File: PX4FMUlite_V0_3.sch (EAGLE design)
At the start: 155 parts, among them J2 DF13-4P-1.25V, J201 DF13C-6P-1.25V, J202 DF13C-6P-1.25V, J203 DF13C-6P-1.25V, J3 DF13C-4P-1.25V, J302 DF13C-4P-1.25V, J401 DF13C-4P-1.25V, J403 DF13C-7P-1.25V, J405 DF13C-4P-1.25V, J801 JST-ZH-3, J802 DF13C-3P-1.25V, M3_MOUNT1101 MOUNT-HOLE3.1MM, M3_MOUNT1102 MOUNT-HOLE3.1MM, M3_MOUNT1103 MOUNT-HOLE3.1MM, M3_MOUNT1104 MOUNT-HOLE3.1MM, U101 STM32F4X7VX, U2 MAX3051, U401 MAX3051, U903 74LVC2G240, X101 3.2x2.5 mm / 24 MHz / 15 ppm

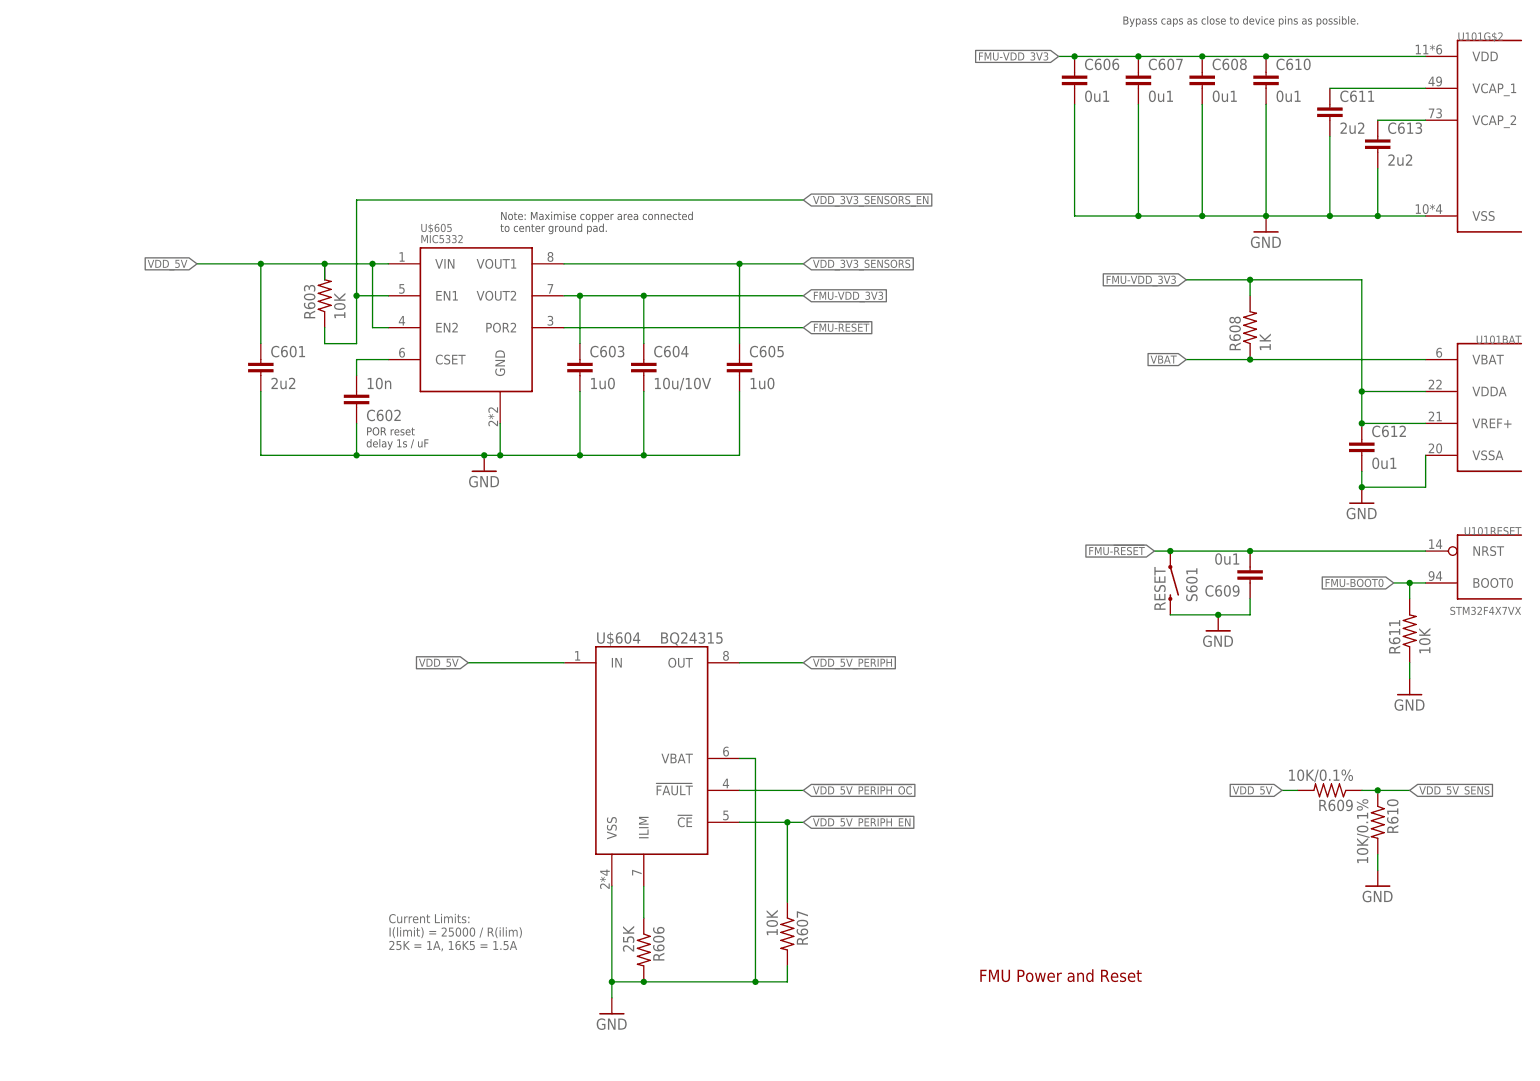
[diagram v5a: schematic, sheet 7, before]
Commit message: LDO shuffle. VBUS reconnected
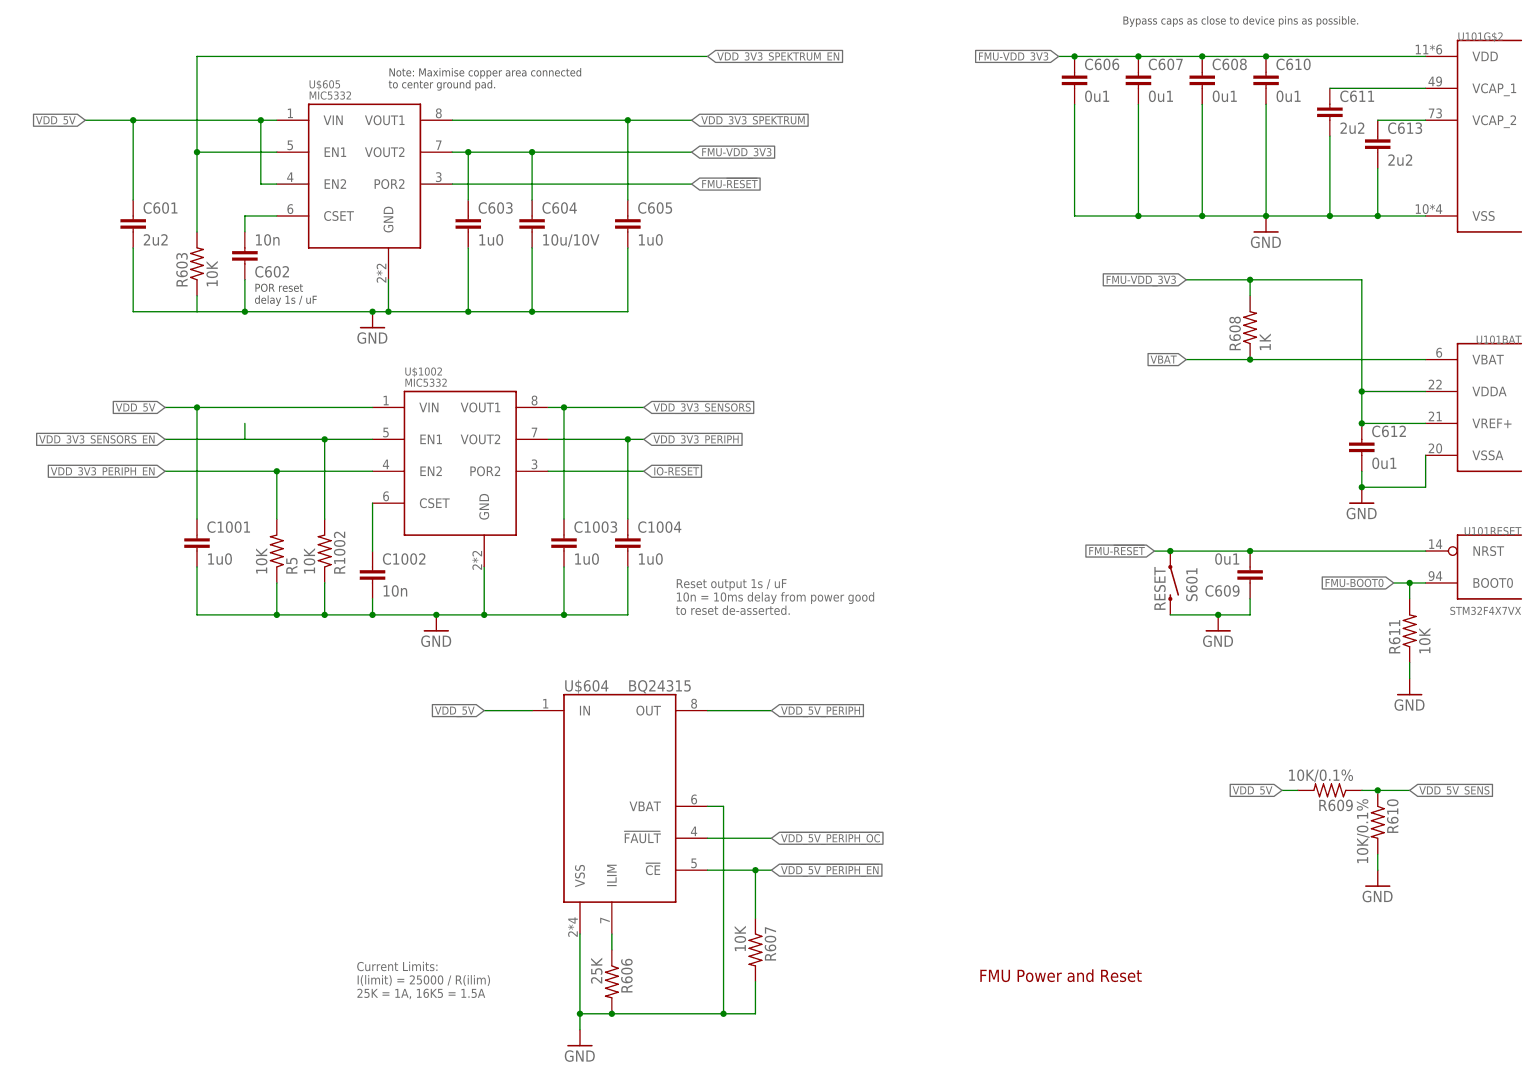
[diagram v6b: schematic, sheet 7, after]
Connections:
- net N$3 renamed V_OR_D
- net V_BUS renamed VBUS
- net GND: now also R603.1
- net VDD_3V3_SENSORS: now also C1003.1, U$1002.VOUT1; no longer C605.1, U$605.VOUT1
- net VDD_3V3_SENSORS_EN: now also R1002.2, U$1002.EN1; no longer R603.1, U$605.EN1
- net VDD_3V3_SPEKTRUM: now also C605.1, U$605.VOUT1; no longer C1003.1, U$1002.VOUT1
- net VDD_3V3_SPEKTRUM_EN: now also R603.2, U$605.EN1; no longer R1002.2, U$1002.EN1
- net VDD_5V: no longer R603.2
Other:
- moved on the sheet: C601, C602, C603, C604, C605, J302, R603, R606, R607, U$604, U$605

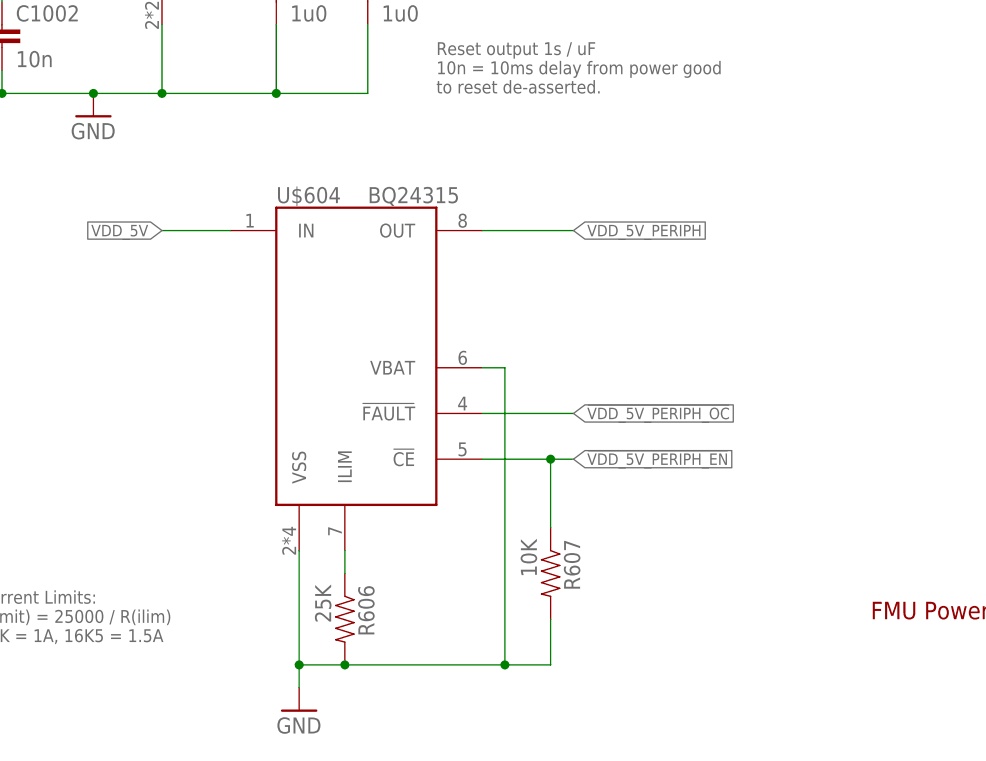
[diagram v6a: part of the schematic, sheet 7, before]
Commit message: Reconnected VDD_5V_PERIPHERAL
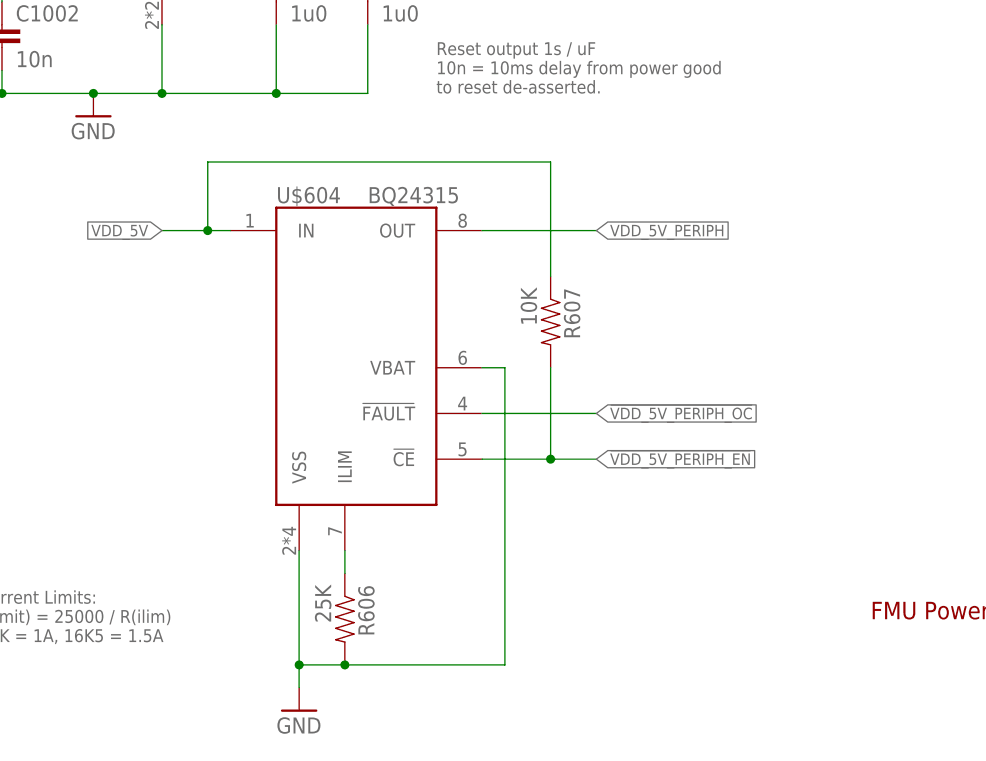
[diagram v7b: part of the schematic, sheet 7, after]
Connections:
- net !VDD_5V_PERIPH_EN: now also R607.2; no longer R607.1
- net GND: no longer R607.2
- net VDD_5V: now also R607.1
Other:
- moved on the sheet: R607
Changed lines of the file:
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@@
-</segment>
-</net>
-<net name="VDD_5V_PERIPH" class="1">
-<segment>
-<pinref part="L203" gate="G$1" pin="P$1"/>
-<wire x1="187.96" y1="86.36" x2="185.42" y2="86.36" width="0.1524" layer="91"/>
-<label x="185.42" y="86.36" size="1.27" layer="95" rot="R180" xref="yes"/>
-</segment>
-<segment>
-<pinref part="L202" gate="G$1" pin="P$1"/>
-<wire x1="187.96" y1="124.46" x2="185.42" y2="124.46" width="0.1524" layer="91"/>
-<label x="185.42" y="124.46" size="1.27" layer="95" rot="R180" xref="yes"/>
-</segment>
-<segment>
-<pinref part="L201" gate="G$1" pin="P$1"/>
-<wire x1="187.96" y1="157.48" x2="185.42" y2="157.48" width="0.1524" layer="91"/>
-<label x="185.42" y="157.48" size="1.27" layer="95" rot="R180" xref="yes"/>
 </segment>
 </net>
@@
 <wire x1="210.82" y1="119.38" x2="210.82" y2="106.68" width="0.1524" layer="91"/>
 <junction x="210.82" y="106.68"/>
+</segment>
+</net>
+<net name="VDD_5V_PERIPH" class="1">
+<segment>
+<pinref part="L203" gate="G$1" pin="P$1"/>
+<wire x1="187.96" y1="86.36" x2="185.42" y2="86.36" width="0.1524" layer="91"/>
+<label x="185.42" y="86.36" size="1.27" layer="95" rot="R180" xref="yes"/>
+</segment>
+<segment>
+<pinref part="L202" gate="G$1" pin="P$1"/>
+<wire x1="187.96" y1="124.46" x2="185.42" y2="124.46" width="0.1524" layer="91"/>
+<label x="185.42" y="124.46" size="1.27" layer="95" rot="R180" xref="yes"/>
+</segment>
+<segment>
+<pinref part="L201" gate="G$1" pin="P$1"/>
+<wire x1="187.96" y1="157.48" x2="185.42" y2="157.48" width="0.1524" layer="91"/>
+<label x="185.42" y="157.48" size="1.27" layer="95" rot="R180" xref="yes"/>
 </segment>
 </net>
@@
 </busses>
 <nets>
-<net name="VDD_5V_PERIPH" class="1">
-<segment>
-<wire x1="55.88" y1="160.02" x2="48.26" y2="160.02" width="0.1524" layer="91"/>
-<label x="48.26" y="160.02" size="1.27" layer="95" rot="R180" xref="yes"/>
-<pinref part="L402" gate="G$1" pin="P$1"/>
-</segment>
-<segment>
-<wire x1="177.8" y1="66.04" x2="139.7" y2="66.04" width="0.1524" layer="91"/>
-<label x="139.7" y="66.04" size="1.27" layer="95" rot="R180" xref="yes"/>
-<pinref part="L403" gate="G$1" pin="P$1"/>
-</segment>
-<segment>
-<wire x1="66.04" y1="114.3" x2="27.94" y2="114.3" width="0.1524" layer="91"/>
-<label x="27.94" y="114.3" size="1.27" layer="95" rot="R180" xref="yes"/>
-<pinref part="L5" gate="G$1" pin="P$1"/>
-</segment>
-<segment>
-<label x="30.48" y="60.96" size="1.27" layer="95" rot="R180" xref="yes"/>
-<wire x1="58.42" y1="60.96" x2="30.48" y2="60.96" width="0.1524" layer="91"/>
-<pinref part="JP3" gate="G$1" pin="3"/>
-<wire x1="55.88" y1="55.88" x2="58.42" y2="55.88" width="0.1524" layer="91"/>
-<wire x1="58.42" y1="55.88" x2="58.42" y2="60.96" width="0.1524" layer="91"/>
-</segment>
-<segment>
-<wire x1="177.8" y1="114.3" x2="139.7" y2="114.3" width="0.1524" layer="91"/>
-<label x="139.7" y="114.3" size="1.27" layer="95" rot="R180" xref="yes"/>
-<pinref part="L7" gate="G$1" pin="P$1"/>
-</segment>
-</net>
 <net name="SPI_EXT_MISO" class="0">
 <segment>
@@
 <wire x1="55.88" y1="50.8" x2="58.42" y2="50.8" width="0.1524" layer="91"/>
 <wire x1="58.42" y1="50.8" x2="58.42" y2="48.26" width="0.1524" layer="91"/>
+</segment>
+</net>
+<net name="VDD_5V_PERIPH" class="1">
+<segment>
+<wire x1="55.88" y1="160.02" x2="48.26" y2="160.02" width="0.1524" layer="91"/>
+<label x="48.26" y="160.02" size="1.27" layer="95" rot="R180" xref="yes"/>
+<pinref part="L402" gate="G$1" pin="P$1"/>
+</segment>
+<segment>
+<wire x1="177.8" y1="114.3" x2="139.7" y2="114.3" width="0.1524" layer="91"/>
+<label x="139.7" y="114.3" size="1.27" layer="95" rot="R180" xref="yes"/>
+<pinref part="L7" gate="G$1" pin="P$1"/>
+</segment>
+<segment>
+<wire x1="177.8" y1="66.04" x2="139.7" y2="66.04" width="0.1524" layer="91"/>
+<label x="139.7" y="66.04" size="1.27" layer="95" rot="R180" xref="yes"/>
+<pinref part="L403" gate="G$1" pin="P$1"/>
+</segment>
+<segment>
+<label x="30.48" y="60.96" size="1.27" layer="95" rot="R180" xref="yes"/>
+<wire x1="58.42" y1="60.96" x2="30.48" y2="60.96" width="0.1524" layer="91"/>
+<pinref part="JP3" gate="G$1" pin="3"/>
+<wire x1="55.88" y1="55.88" x2="58.42" y2="55.88" width="0.1524" layer="91"/>
+<wire x1="58.42" y1="55.88" x2="58.42" y2="60.96" width="0.1524" layer="91"/>
+</segment>
+<segment>
+<wire x1="66.04" y1="114.3" x2="27.94" y2="114.3" width="0.1524" layer="91"/>
+<label x="27.94" y="114.3" size="1.27" layer="95" rot="R180" xref="yes"/>
+<pinref part="L5" gate="G$1" pin="P$1"/>
 </segment>
 </net>
@@
 </instance>
 <instance part="GND39" gate="1" x="101.6" y="7.62"/>
-<instance part="R607" gate="G$1" x="129.54" y="22.86" rot="R270">
-<attribute name="PARTNO" x="129.54" y="22.86" size="1.778" layer="96" rot="R90" display="off"/>
+<instance part="R607" gate="G$1" x="129.54" y="50.8" rot="R270">
+<attribute name="PARTNO" x="129.54" y="50.8" size="1.778" layer="96" rot="R90" display="off"/>
 </instance>
 <instance part="U$605" gate="G$1" x="66.04" y="149.86">
@@
 <wire x1="101.6" y1="12.7" x2="101.6" y2="10.16" width="0.1524" layer="91"/>
 <junction x="106.68" y="12.7"/>
-<pinref part="R607" gate="G$1" pin="2"/>
-<wire x1="129.54" y1="17.78" x2="129.54" y2="12.7" width="0.1524" layer="91"/>
-<wire x1="129.54" y1="12.7" x2="124.46" y2="12.7" width="0.1524" layer="91"/>
 <pinref part="R606" gate="G$1" pin="2"/>
 <pinref part="U$604" gate="G$1" pin="VBAT"/>
@@
 <wire x1="121.92" y1="45.72" x2="124.46" y2="45.72" width="0.1524" layer="91"/>
 <wire x1="124.46" y1="45.72" x2="124.46" y2="12.7" width="0.1524" layer="91"/>
-<junction x="124.46" y="12.7"/>
 <pinref part="U$604" gate="G$1" pin="VSS"/>
 <wire x1="101.6" y1="25.4" x2="101.6" y2="12.7" width="0.1524" layer="91"/>
@@
 <segment>
 <pinref part="U$604" gate="G$1" pin="IN"/>
-<wire x1="93.98" y1="60.96" x2="86.36" y2="60.96" width="0.1524" layer="91"/>
+<wire x1="93.98" y1="60.96" x2="91.44" y2="60.96" width="0.1524" layer="91"/>
 <label x="86.36" y="60.96" size="1.27" layer="95" rot="R180" xref="yes"/>
+<pinref part="R607" gate="G$1" pin="1"/>
+<wire x1="91.44" y1="60.96" x2="86.36" y2="60.96" width="0.1524" layer="91"/>
+<wire x1="129.54" y1="55.88" x2="129.54" y2="68.58" width="0.1524" layer="91"/>
+<wire x1="129.54" y1="68.58" x2="91.44" y2="68.58" width="0.1524" layer="91"/>
+<wire x1="91.44" y1="68.58" x2="91.44" y2="60.96" width="0.1524" layer="91"/>
+<junction x="91.44" y="60.96"/>
 </segment>
 <segment>
@@
 <segment>
 <wire x1="121.92" y1="35.56" x2="129.54" y2="35.56" width="0.1524" layer="91"/>
-<label x="132.08" y="35.56" size="1.27" layer="95" xref="yes"/>
-<wire x1="129.54" y1="35.56" x2="132.08" y2="35.56" width="0.1524" layer="91"/>
+<label x="134.62" y="35.56" size="1.27" layer="95" xref="yes"/>
+<pinref part="U$604" gate="G$1" pin="!CE"/>
+<pinref part="R607" gate="G$1" pin="2"/>
+<wire x1="129.54" y1="35.56" x2="134.62" y2="35.56" width="0.1524" layer="91"/>
+<wire x1="129.54" y1="45.72" x2="129.54" y2="35.56" width="0.1524" layer="91"/>
 <junction x="129.54" y="35.56"/>
-<pinref part="R607" gate="G$1" pin="1"/>
-<wire x1="129.54" y1="27.94" x2="129.54" y2="35.56" width="0.1524" layer="91"/>
-<pinref part="U$604" gate="G$1" pin="!CE"/>
 </segment>
 </net>
@@
 <net name="VDD_5V_PERIPH" class="1">
 <segment>
-<wire x1="121.92" y1="60.96" x2="132.08" y2="60.96" width="0.1524" layer="91"/>
-<label x="132.08" y="60.96" size="1.27" layer="95" xref="yes"/>
+<wire x1="121.92" y1="60.96" x2="134.62" y2="60.96" width="0.1524" layer="91"/>
+<label x="134.62" y="60.96" size="1.27" layer="95" xref="yes"/>
 <pinref part="U$604" gate="G$1" pin="OUT"/>
 </segment>
@@
 <net name="!VDD_5V_PERIPH_OC" class="0">
 <segment>
-<label x="132.08" y="40.64" size="1.27" layer="95" xref="yes"/>
-<wire x1="121.92" y1="40.64" x2="132.08" y2="40.64" width="0.1524" layer="91"/>
+<label x="134.62" y="40.64" size="1.27" layer="95" xref="yes"/>
+<wire x1="121.92" y1="40.64" x2="134.62" y2="40.64" width="0.1524" layer="91"/>
 <pinref part="U$604" gate="G$1" pin="!FAULT"/>
 </segment>
@@
 </segment>
 </net>
-<net name="VDD_3V3_PERIPH" class="1">
-<segment>
-<label x="111.76" y="104.14" size="1.27" layer="95" xref="yes"/>
-<wire x1="109.22" y1="104.14" x2="111.76" y2="104.14" width="0.1524" layer="91"/>
-<pinref part="C1004" gate="G$1" pin="1"/>
-<wire x1="109.22" y1="91.44" x2="109.22" y2="104.14" width="0.1524" layer="91"/>
-<pinref part="U$1002" gate="G$1" pin="VOUT2"/>
-<wire x1="109.22" y1="104.14" x2="96.52" y2="104.14" width="0.1524" layer="91"/>
-<junction x="109.22" y="104.14"/>
-</segment>
-</net>
 <net name="N$104" class="0">
 <segment>
@@
 </segment>
 </net>
+<net name="VDD_3V3_PERIPH" class="1">
+<segment>
+<label x="111.76" y="104.14" size="1.27" layer="95" xref="yes"/>
+<wire x1="109.22" y1="104.14" x2="111.76" y2="104.14" width="0.1524" layer="91"/>
+<pinref part="C1004" gate="G$1" pin="1"/>
+<wire x1="109.22" y1="91.44" x2="109.22" y2="104.14" width="0.1524" layer="91"/>
+<pinref part="U$1002" gate="G$1" pin="VOUT2"/>
+<wire x1="109.22" y1="104.14" x2="96.52" y2="104.14" width="0.1524" layer="91"/>
+<junction x="109.22" y="104.14"/>
+</segment>
+</net>
